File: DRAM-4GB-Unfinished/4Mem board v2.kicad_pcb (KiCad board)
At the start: 6 copper layers, 150.4 x 75.2 mm, 29 parts, among them P1 CONN_1, P11 CONN_2X2, P2 CONN_1, P3 CONN_1, P4 CONN_1, P8 CONN_20X2, P9 CONN_20X2, U1 XC6SLX45-2FGG484C, U2 DDR3_DIMM_240PIN, U7 LM1086CS_TO252_DPAK

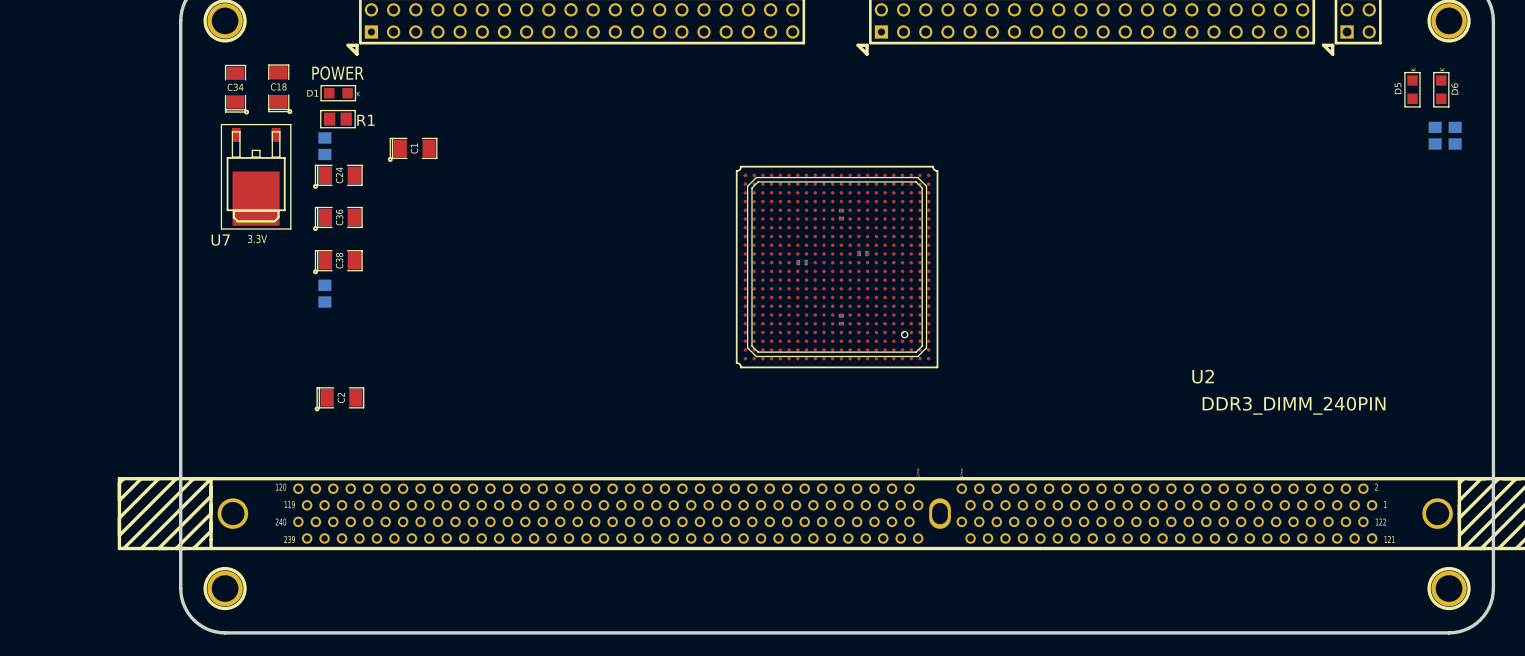
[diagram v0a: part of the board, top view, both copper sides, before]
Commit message: DRAM-4GB-Unfinished: add regulators, P8/P9 I/O nets, start BGA fanout
Source: S100 4GB DRAM BOARD/4Mem board v2/backups/09-05-2015 1716
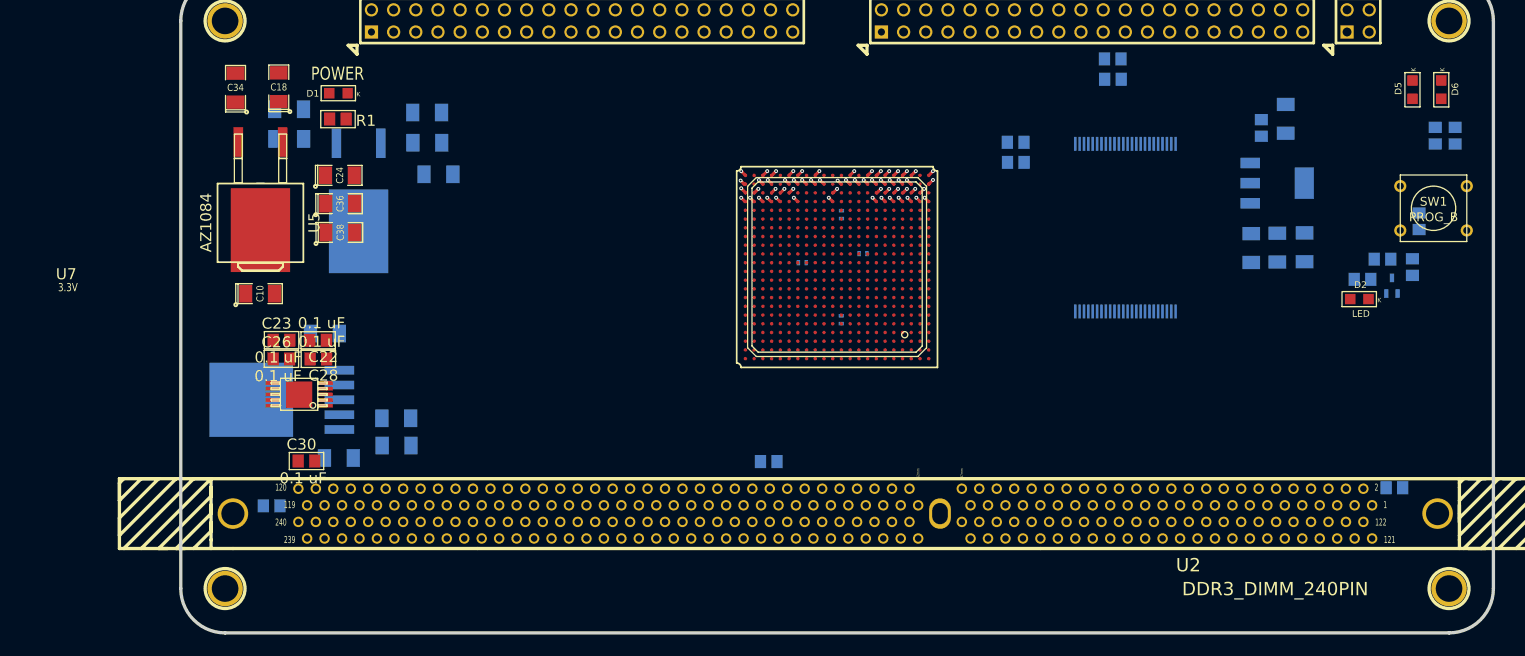
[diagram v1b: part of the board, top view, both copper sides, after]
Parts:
- removed C1, C2: 10 uF, SM1206_Opendous
- added C10: 10 uF, SM1206_Opendous, F.Cu at (113.6, 113.8)
- added C11: 10 uF, SM1206_Opendous, B.Cu at (233.3, 108.5)
- added C12: 10 uF, SM1206_Opendous, B.Cu at (134.0, 100.1)
- added C13: 10 uF, SM1206_Opendous, B.Cu at (129.2, 131.2)
- added C15: 10 uF, SM1206_Opendous, B.Cu at (230.1, 108.5)
- added C16: 10 uF, SM1206_Opendous, B.Cu at (132.7, 93.0)
- added C17: 10 uF, SM1206_Opendous, B.Cu at (129.2, 128.1)
- added C19: 10 uF, SM1206_Opendous, B.Cu at (227.1, 108.6)
- added C20: 10 uF, SM1206_Opendous, B.Cu at (132.8, 96.5)
- added C21: 10 uF, SM1206_Opendous, B.Cu at (122.6, 132.6)
- added C22: 0.1 uF, ^^SMD_Resistor-0805, F.Cu at (120.3, 119.1)
- added C23: 0.1 uF, ^^SMD_Resistor-0805, F.Cu at (116.1, 119.1)
- added C25: 0.1 uF, ^^SMD_Resistor-0805, B.Cu at (114.9, 138.1)
- added C26: 0.1 uF, ^^SMD_Resistor-0805, F.Cu at (116.0, 121.3)
- added C28: 0.1 uF, ^^SMD_Resistor-0805, F.Cu at (120.3, 121.3)
- added C29: 0.1 uF, ^^SMD_Resistor-0805, B.Cu at (243.6, 136.0)
- added C31: 0.1 uF, ^^SMD_Resistor-0805, B.Cu at (171.9, 133.0)
- added C5: 10 uF, SM1206_Opendous, B.Cu at (116.9, 96.1)
- added C7: 10 uF, SM1206_Opendous, B.Cu at (121.0, 118.4)
- added C8: 10 uF, SM1206_Opendous, B.Cu at (231.1, 93.8)
- added C9: 10 uF, SM1206_Opendous, B.Cu at (116.9, 92.7)
- added D2: LED, ^^LED-0805, F.Cu at (239.5, 114.4)
- added Q1: ^^NPN-BC817-SOT323, -SOT323, B.Cu at (243.3, 112.9)
- added R10: 4K7, ^^SMD_Resistor-0805, B.Cu at (246.4, 105.5)
- added R11: 330, ^^SMD_Resistor-0805, B.Cu at (242.2, 109.8)
- added R2: 330, ^^SMD_Resistor-0805, B.Cu at (239.9, 112.2)
- added R3: 4K7, ^^SMD_Resistor-0805, B.Cu at (200.2, 98.8)
- added R4: 4K7, ^^SMD_Resistor-0805, B.Cu at (200.2, 96.5)
- added R7: 4K7, ^^SMD_Resistor-0805, B.Cu at (211.3, 89.2)
- added R8: 0, ^^SMD_Resistor-0805, B.Cu at (245.6, 110.8)
- added R9: 4K7, ^^SMD_Resistor-0805, B.Cu at (211.3, 86.9)
- added SW1: PROG_B, SW_PUSH_SMALL, F.Cu at (248.0, 104.0)
- added U3: XCF08P-VO48/TSOP48, ^^TSOP48, B.Cu at (212.7, 106.2)
- added U4: LM1117MP-1.8, ^^SOT223v1, B.Cu at (230.1, 101.1)
- added U5: AZ1084, ^^TO263-3pin+tab, F.Cu at (113.7, 103.0)
- added U6: NCP565, ^^TO263-3pin+tab, B.Cu at (124.9, 103.2)
- added U8: RT9026_MSOP-10, ^^RT9026_MSOP10, F.Cu at (118.1, 124.4)
- C3: value 0.1 uF -> 10 uF
- C30: moved to F.Cu
- U7: value LM1086CS_TO252_DPAK -> LT1764EQ-1.5; footprint -TO252 -> ^^TO263-51; moved to B.Cu
- moved C3 107.3 mm to (228.3, 94.8)
- moved U7 25.7 mm to (116.1, 126.0), turned to 270 degrees
- moved C30 19.3 mm to (118.9, 133.0), turned to 0 degrees
- moved C38 3.24 mm to (122.8, 106.8)
- moved C36 1.59 mm to (122.8, 103.5)
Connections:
- net /V1.2 renamed /V1.2temp
- C14 pad 1: /V3.3 -> /V3.3b
- C27 pad 1: /V3.3 -> /V3.3b
- C3 pad 1: /V3.3 -> /+8Vitemp
- C30 pad 1: /V3.3 -> /DDR3_VTT
- C4 pad 1: /V3.3 -> /V3.3b
- C6 pad 1: /V3.3 -> /V3.3b
- P11 pad 1: (no net) -> /PF_TDO
- P11 pad 2: (no net) -> /mm_TMS
- P11 pad 3: (no net) -> /FPGA_TDI
- P11 pad 4: (no net) -> /mm_TCK
- P8 pad 10: (no net) -> /IO_096
- P8 pad 12: (no net) -> /IO_097
- P8 pad 14: (no net) -> /IO_098
- P8 pad 16: (no net) -> /IO_099
- P8 pad 18: (no net) -> /IO_100
- P8 pad 20: (no net) -> /IO_101
- P8 pad 22: (no net) -> /IO_102
- P8 pad 24: (no net) -> /IO_103
- P8 pad 26: (no net) -> /IO_104
- P8 pad 28: (no net) -> /IO_105
- P8 pad 30: (no net) -> /IO_106
- P8 pad 32: (no net) -> /IO_107
- P8 pad 34: (no net) -> /IO_108
- P8 pad 36: (no net) -> /IO_109
- P8 pad 38: (no net) -> /IO_090
- P8 pad 40: (no net) -> /IO_091
- P8 pad 6: (no net) -> /IO_094
- P8 pad 8: (no net) -> /IO_095
- P9 pad 10: (no net) -> /IO_086
- P9 pad 12: (no net) -> /IO_087
- P9 pad 14: (no net) -> /IO_088
- P9 pad 16: (no net) -> /IO_089
- P9 pad 2: (no net) -> /IO_092
- P9 pad 4: (no net) -> /IO_093
- P9 pad 6: (no net) -> /IO_084
- P9 pad 8: (no net) -> /IO_085
- U1 pad A19: (no net) -> /FPGA_TDO
- U1 pad A3: (no net) -> GND
- U1 pad AA1: (no net) -> /FPGA_PROGRAM_B
- U1 pad AA10: (no net) -> /IO_091
- U1 pad AA11: (no net) -> /V3.3temp
- U1 pad AA14: (no net) -> /IO_098
- U1 pad AA15: (no net) -> /V3.3temp
- U1 pad AA16: (no net) -> /IO_096
- U1 pad AA19: (no net) -> /V3.3temp
- U1 pad AA20: (no net) -> /PF_D0
- U1 pad AA22: (no net) -> GND
- U1 pad AA3: (no net) -> /V3.3temp
- U1 pad AA4: (no net) -> /IO_093
- U1 pad AA6: (no net) -> /PF_D3
- U1 pad AA7: (no net) -> /V3.3temp
- U1 pad AA8: (no net) -> /IO_109
- U1 pad AB10: (no net) -> /IO_090
- U1 pad AB14: (no net) -> /IO_099
- U1 pad AB16: (no net) -> /IO_097
- U1 pad AB17: (no net) -> /IO_103
- U1 pad AB19: (no net) -> /IO_101
- U1 pad AB20: (no net) -> GND
- U1 pad AB3: (no net) -> /IO_086
- U1 pad AB4: (no net) -> /IO_092
- U1 pad AB5: (no net) -> /IO_084
- U1 pad AB6: (no net) -> /PF_D4
- U1 pad AB7: (no net) -> GND
- U1 pad AB8: (no net) -> /IO_108
- U1 pad B11: (no net) -> /V3.3temp
- U1 pad B15: (no net) -> /V3.3temp
- U1 pad B19: (no net) -> /V3.3temp
- U1 pad B4: (no net) -> /V3.3temp
- U1 pad B7: (no net) -> /V3.3temp
- U1 pad C18: (no net) -> /mm_TMS
- U1 pad C2: (no net) -> /V1.5temp
- U1 pad C21: (no net) -> /V1.5temp
- U1 pad D16: /V3.3 -> /V3.3temp
- U1 pad E13: (no net) -> /V3.3temp
- U1 pad E17: (no net) -> /V3.3temp
- U1 pad E18: (no net) -> /FPGA_TDI
- U1 pad E19: (no net) -> /V1.5temp
- U1 pad E9: (no net) -> /V3.3temp
- U1 pad F11: /V3.3 -> /V3.3temp
- U1 pad F4: (no net) -> /V1.5temp
- U1 pad F6: (no net) -> /V1.5temp
- U1 pad G10: (no net) -> /V3.3temp
- U1 pad G12: /V3.3 -> /V3.3temp
- U1 pad G14: (no net) -> /V3.3temp
- U1 pad G15: (no net) -> /mm_TCK
- U1 pad G2: (no net) -> /V1.5temp
- U1 pad G21: (no net) -> /V1.5temp
- U1 pad H15: /V3.3 -> /V3.3temp
- U1 pad H9: /V3.3 -> /V3.3temp
- U1 pad J18: (no net) -> /V1.5temp
- U1 pad J5: (no net) -> /V1.5temp
- U1 pad K15: /V3.3 -> /V3.3temp
- U1 pad L16: (no net) -> /V1.5temp
- U1 pad L2: (no net) -> /V1.5temp
- U1 pad L21: (no net) -> /V1.5temp
- U1 pad L7: (no net) -> /V1.5temp
- U1 pad L8: /V3.3 -> /V3.3temp
- U1 pad M15: /V3.3 -> /V3.3temp
- U1 pad N15: (no net) -> GND
- U1 pad N18: (no net) -> /V1.5temp
- U1 pad N5: (no net) -> /V1.5temp
- U1 pad N8: /V3.3 -> /V3.3temp
- U1 pad R10: /V3.3 -> /V3.3temp
- U1 pad R12: /V3.3 -> /V3.3temp
- U1 pad R2: (no net) -> /V1.5temp
- U1 pad R21: (no net) -> /V1.5temp
- U1 pad R6: /V3.3 -> /V3.3temp
- U1 pad T13: (no net) -> /V3.3temp
- U1 pad T6: (no net) -> /FPGA_INIT_B
- U1 pad T9: (no net) -> /V3.3temp
- U1 pad U11: /V3.3 -> /V3.3temp
- U1 pad U13: (no net) -> /PF_D2
- U1 pad U14: (no net) -> /PF_D1
- U1 pad U15: (no net) -> GND
- U1 pad U18: (no net) -> /V1.5temp
- U1 pad U5: (no net) -> /V1.5temp
- U1 pad U6: (no net) -> /IO_106
- U1 pad V12: (no net) -> /V3.3temp
- U1 pad V16: (no net) -> /V3.3temp
- U1 pad V5: (no net) -> /IO_107
- U1 pad V6: /V3.3 -> /V3.3temp
- U1 pad V8: (no net) -> /V3.3temp
- U1 pad W12: (no net) -> /IO_094
- U1 pad W18: (no net) -> /IO_104
- U1 pad W2: (no net) -> /V1.5temp
- U1 pad W21: (no net) -> /V1.5temp
- U1 pad W4: (no net) -> /PF_D5
- U1 pad W5: (no net) -> /V3.3temp
- U1 pad W6: (no net) -> /IO_089
- U1 pad Y12: (no net) -> /IO_095
- U1 pad Y17: (no net) -> /IO_102
- U1 pad Y18: (no net) -> /IO_105
- U1 pad Y19: (no net) -> /IO_100
- U1 pad Y21: (no net) -> /FPGA_CCLK_2
- U1 pad Y22: (no net) -> /FPGA_DONE
- U1 pad Y3: (no net) -> /IO_087
- U1 pad Y4: (no net) -> /PF_D6
- U1 pad Y5: (no net) -> /IO_085
- U1 pad Y6: (no net) -> /IO_088
- U1 pad Y7: (no net) -> /PF_D7
- U2 pad 1: (no net) -> /DDR3_VREF
- U2 pad 120: (no net) -> /DDR3_VTT
- U2 pad 240: (no net) -> /DDR3_VTT
- U2 pad 67: (no net) -> /DDR3_VREF
- U7 pad 1: GND -> /+8Vi
- U7 pad 3: /V3.3 -> GND
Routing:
- net GND: track 0.00 -> 8.12 mm, vias 0 -> 12
- net /V3.3temp: track 0.00 -> 3.99 mm, vias 0 -> 6
- net /V1.5temp: track 0.00 -> 1.26 mm, vias 0 -> 2
- net /IO_086: track 0.00 -> 0.72 mm, vias 0 -> 1
- net /FPGA_DONE: track 0.00 -> 0.72 mm, vias 0 -> 1
- net /IO_101: track 0.00 -> 0.72 mm, vias 0 -> 1
- net /PF_D7: track 0.00 -> 0.71 mm, vias 0 -> 1
- net /IO_092: track 0.00 -> 0.70 mm, vias 0 -> 1
- net /IO_108: track 0.00 -> 0.70 mm, vias 0 -> 1
- net /IO_097: track 0.00 -> 0.70 mm, vias 0 -> 1
- net /PF_D6: track 0.00 -> 0.69 mm, vias 0 -> 1
- net /IO_084: track 0.00 -> 0.69 mm, vias 0 -> 1
- net /IO_103: track 0.00 -> 0.69 mm, vias 0 -> 1
- net /IO_095: track 0.00 -> 0.69 mm, vias 0 -> 1
- net /PF_D4: track 0.00 -> 0.68 mm, vias 0 -> 1
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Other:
- net class Default: clearance 0.1016 -> 0.13; trace_width 0.1524 -> 0.18; via_dia 0.4064 -> 0.45
- net class Power: clearance 0.1016 -> 0.13; trace_width 0.45 -> 0.35; via_dia 0.4064 -> 0.45
- net class Power Bottom: clearance 0.1016 -> 0.13; trace_width 0.305 -> 0.35; via_dia 0.4064 -> 0.45
- net class gnd: clearance 0.1016 -> 0.13; trace_width 0.45 -> 0.15; via_dia 0.4064 -> 0.45
- rule trace_clearance: 0.1016 -> 0.13
- rule trace_min: 0.15 -> 0.1

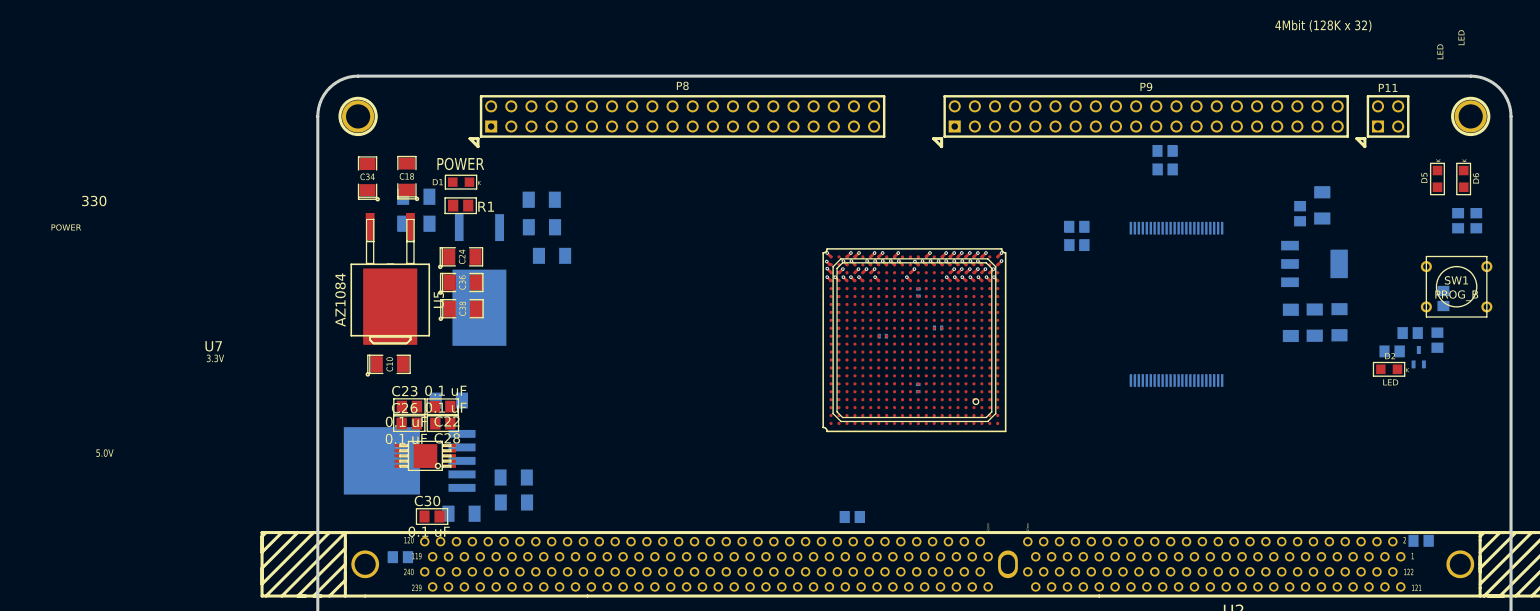
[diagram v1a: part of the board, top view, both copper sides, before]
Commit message: DRAM-4GB-Unfinished: connect all P8/P9 signals to the FPGA; BGA power fanout
Source: S100 4GB DRAM BOARD/4Mem board v2/backups/23-05-2015 2046 (newest file is 2015-05-17)
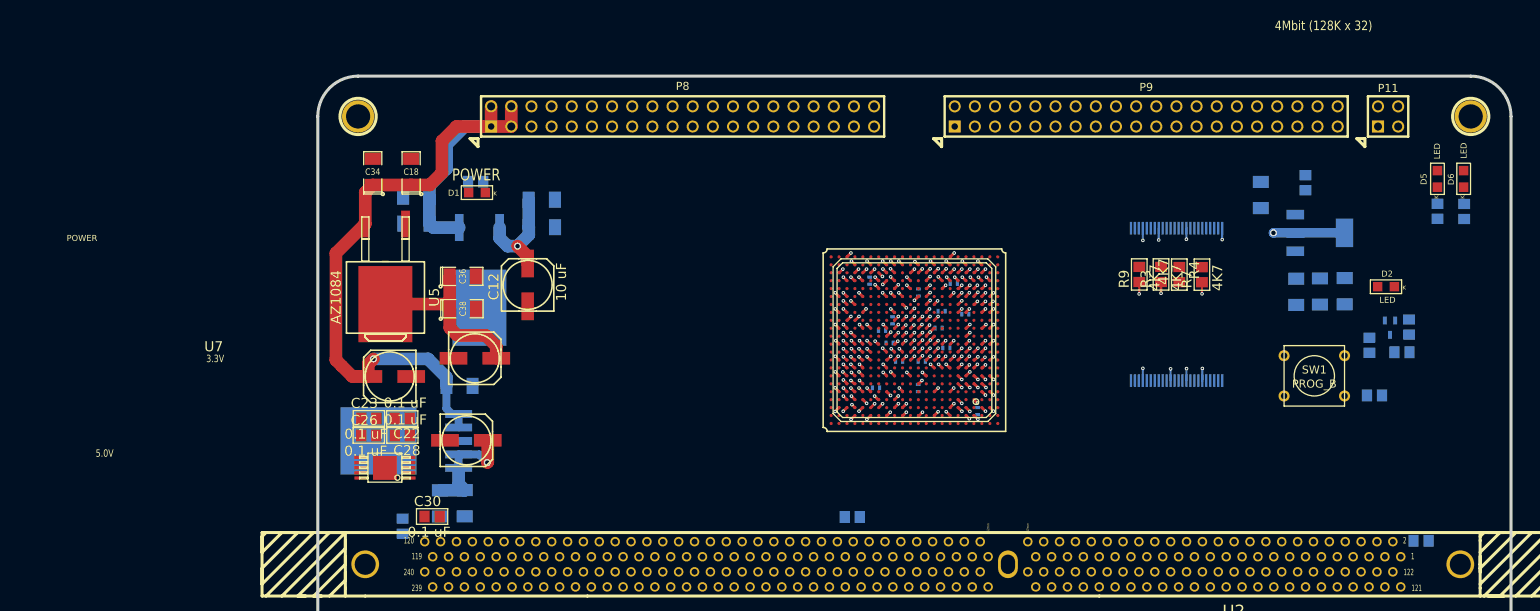
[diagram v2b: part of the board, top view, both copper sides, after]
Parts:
- added C1: 0.1 uF, SM0402_c, B.Cu at (184.7, 103.6)
- added C2: 0.1 uF, SM0402_c, B.Cu at (183.7, 111.7)
- added C32: 0.1 uF, SM0402_c, B.Cu at (174.9, 116.8)
- added C33: 0.1 uF, SM0402_c, B.Cu at (183.1, 107.1)
- added C35: 0.1 uF, SM0402_c, B.Cu at (186.1, 107.5)
- added C37: 0.1 uF, SM0402_c, B.Cu at (180.6, 113.4)
- added C39: 0.1 uF, SM0402_c, B.Cu at (174.1, 103.3)
- added C40: 0.1 uF, SM0402_c, B.Cu at (177.8, 113.4)
- added C41: 0.1 uF, SM0402_c, B.Cu at (176.9, 108.2)
- added C42: 0.1 uF, SM0402_c, B.Cu at (187.7, 119.7)
- added C43: 0.1 uF, SM0402_c, B.Cu at (176.6, 111.1)
- C10, C24: footprint SM1206_Opendous -> ^^153CLV-0605
- C12, C21: footprint SM1206_Opendous -> ^^153CLV-0605; moved to F.Cu
- R1: moved to B.Cu
- R3, R4, R7, R9: moved to F.Cu
- moved SW1 21.2 mm to (230.1, 115.2)
- moved R9 15.9 mm to (208.0, 102.5), turned to 90 degrees
- moved R10 15.0 mm to (237.7, 117.7), turned to 180 degrees
- moved R4 14.3 mm to (213.1, 102.5), turned to 270 degrees
- moved R7 14.0 mm to (215.9, 102.5), turned to 90 degrees
- moved C24 12.9 mm to (124.3, 113.0)
- moved R3 11.2 mm to (210.8, 102.5), turned to 90 degrees
- moved D2 10.4 mm to (239.1, 104.0)
- moved C13 9.32 mm to (119.9, 131.3), turned to 270 degrees
- moved C21 9.27 mm to (123.2, 123.4), turned to 0 degrees
- moved R8 8.60 mm to (237.0, 111.4), turned to 270 degrees
- moved C8 7.85 mm to (223.4, 92.5)
- moved C17 6.96 mm to (123.0, 131.3), turned to 270 degrees
- moved C22 5.32 mm to (115.2, 120.6)
- moved C23 5.32 mm to (111.0, 120.6)
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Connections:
- C14 pad 1: /V3.3b -> /V3.3temp
- C27 pad 1: /V3.3b -> /V3.3temp
- C4 pad 1: /V3.3b -> /V3.3temp
- C6 pad 1: /V3.3b -> /V3.3temp
- P8 pad 11: (no net) -> /IO_075
- P8 pad 13: (no net) -> /IO_000
- P8 pad 15: (no net) -> /IO_001
- P8 pad 17: (no net) -> /IO_002
- P8 pad 19: (no net) -> /IO_003
- P8 pad 21: (no net) -> /IO_004
- P8 pad 23: (no net) -> /IO_005
- P8 pad 25: (no net) -> /IO_006
- P8 pad 27: (no net) -> /IO_007
- P8 pad 29: (no net) -> /IO_008
- P8 pad 31: (no net) -> /IO_009
- P8 pad 33: (no net) -> /IO_010
- P8 pad 35: (no net) -> /IO_011
- P8 pad 37: (no net) -> /IO_012
- P8 pad 39: (no net) -> /IO_013
- P8 pad 5: (no net) -> /IO_072
- P8 pad 7: (no net) -> /IO_073
- P8 pad 9: (no net) -> /IO_074
- P9 pad 1: (no net) -> /IO_014
- P9 pad 11: (no net) -> /IO_019
- P9 pad 13: (no net) -> /IO_020
- P9 pad 15: (no net) -> /IO_021
- P9 pad 17: (no net) -> /IO_022
- P9 pad 18: (no net) -> /IO_076
- P9 pad 19: (no net) -> /IO_023
- P9 pad 20: (no net) -> /IO_077
- P9 pad 21: (no net) -> /IO_024
- P9 pad 22: (no net) -> /IO_078
- P9 pad 23: (no net) -> /IO_025
- P9 pad 24: (no net) -> /IO_079
- P9 pad 25: (no net) -> /IO_026
- P9 pad 26: (no net) -> /IO_080
- P9 pad 27: (no net) -> /IO_027
- P9 pad 28: (no net) -> /IO_081
- P9 pad 29: (no net) -> /IO_028
- P9 pad 3: (no net) -> /IO_015
- P9 pad 30: (no net) -> /IO_082
- P9 pad 31: (no net) -> /IO_029
- P9 pad 32: (no net) -> /IO_083
- P9 pad 33: (no net) -> /IO_030
- P9 pad 34: (no net) -> /IO_033
- P9 pad 35: (no net) -> /IO_031
- P9 pad 36: (no net) -> /IO_034
- P9 pad 37: (no net) -> /IO_032
- P9 pad 38: (no net) -> /IO_035
- P9 pad 5: (no net) -> /IO_016
- P9 pad 7: (no net) -> /IO_017
- P9 pad 9: (no net) -> /IO_018
- R10 pad 1: /V3.3 -> /V3.3temp
- R11 pad 1: /V3.3 -> /V3.3temp
- R2 pad 1: /V3.3 -> /V3.3temp
- R3 pad 1: /V3.3 -> /V3.3temp2
- R7 pad 1: /V3.3 -> /V3.3temp2
- R9 pad 1: /V3.3 -> /V3.3temp2
- U1 pad A10: (no net) -> /IO_015
- U1 pad A12: (no net) -> /IO_023
- U1 pad A13: (no net) -> /IO_025
- U1 pad A14: (no net) -> /IO_001
- U1 pad A16: (no net) -> /IO_004
- U1 pad A17: (no net) -> /IO_002
- U1 pad A5: (no net) -> /IO_034
- U1 pad A6: (no net) -> /IO_009
- U1 pad A7: (no net) -> /IO_011
- U1 pad A8: (no net) -> /IO_013
- U1 pad AA12: (no net) -> /IO_081
- U1 pad AA18: (no net) -> /IO_072
- U1 pad AB11: (no net) -> /IO_082
- U1 pad AB12: (no net) -> /IO_080
- U1 pad AB15: (no net) -> /IO_079
- U1 pad AB18: (no net) -> /IO_073
- U1 pad AB9: (no net) -> /IO_016
- U1 pad B10: (no net) -> /IO_014
- U1 pad B12: (no net) -> /IO_022
- U1 pad B14: (no net) -> /IO_000
- U1 pad B16: (no net) -> /IO_007
- U1 pad B18: (no net) -> /IO_003
- U1 pad B6: (no net) -> /IO_008
- U1 pad B8: (no net) -> /IO_012
- U1 pad C13: (no net) -> /IO_024
- U1 pad C14: (no net) -> /IO_027
- U1 pad C16: (no net) -> /IO_006
- U1 pad C17: (no net) -> /IO_005
- U1 pad C5: (no net) -> /IO_035
- U1 pad C6: (no net) -> /IO_032
- U1 pad C7: (no net) -> /IO_010
- U1 pad D14: (no net) -> /IO_026
- U1 pad D6: (no net) -> /IO_033
- U1 pad T10: (no net) -> /IO_075
- U1 pad U10: (no net) -> /IO_074
- U1 pad U16: (no net) -> /IO_028
- U1 pad U17: (no net) -> /IO_029
- U1 pad W10: (no net) -> /IO_019
- U1 pad W14: (no net) -> /IO_076
- U1 pad W15: (no net) -> /IO_021
- U1 pad W8: (no net) -> /IO_030
- U1 pad Y10: (no net) -> /IO_018
- U1 pad Y11: (no net) -> /IO_083
- U1 pad Y14: (no net) -> /IO_077
- U1 pad Y15: (no net) -> /IO_078
- U1 pad Y16: (no net) -> /IO_020
- U1 pad Y8: (no net) -> /IO_031
- U1 pad Y9: (no net) -> /IO_017
- U3 pad 24: /V3.3 -> /V3.3temp2
- U3 pad 30: /V3.3 -> /V3.3temp2
- U3 pad 38: /V3.3 -> /V3.3temp2
- U3 pad 45: /V3.3 -> /V3.3temp2
- U3 pad 8: /V3.3 -> /V3.3temp2
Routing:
- net /+8Vi: track 0.00 -> 98.4 mm, vias 0 -> 1
- net GND: track 8.12 -> 38.6 mm, vias 12 -> 57
- net /V3.3: track 0.00 -> 23.2 mm
- net /V3.3temp: track 3.99 -> 22.6 mm, vias 6 -> 34
- net /V1.5: track 0.00 -> 15.9 mm, vias 0 -> 1
- net /V1.8: track 0.00 -> 13.4 mm, vias 0 -> 4
- net /V1.2temp: track 0.00 -> 13.3 mm, vias 0 -> 19
- net /V1.2: track 0.00 -> 13.2 mm, vias 0 -> 1
- net /V3.3temp2: track 0.00 -> 11.9 mm, vias 0 -> 8
- net /V1.5temp: track 1.26 -> 13.1 mm, vias 2 -> 20
- net /DDR3_DQS0h: track 0.00 -> 0.74 mm, vias 0 -> 1
- net /DDR3_DQ45: track 0.00 -> 0.72 mm, vias 0 -> 1
- net /IO_086: track 0.72 -> 0.00 mm, vias 1 -> 0
- net /FPGA_DONE: track 0.72 -> 0.00 mm, vias 1 -> 0
- net /IO_019: track 0.00 -> 0.72 mm, vias 0 -> 1
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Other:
- net class Default: clearance 0.13 -> 0.11; trace_width 0.18 -> 0.15
- net class Power: clearance 0.13 -> 0.11; trace_width 0.35 -> 0.26
- net class Power Bottom: clearance 0.13 -> 0.11; trace_width 0.35 -> 0.26
- net class gnd: clearance 0.13 -> 0.11
- rule trace_clearance: 0.13 -> 0.11
